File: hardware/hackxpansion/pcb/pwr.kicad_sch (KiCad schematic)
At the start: 18 parts, among them Q2 2N7002, SW3 SW_On_Off, U5 SPX3819M5-L-3-3, U7 BQ24075RGT

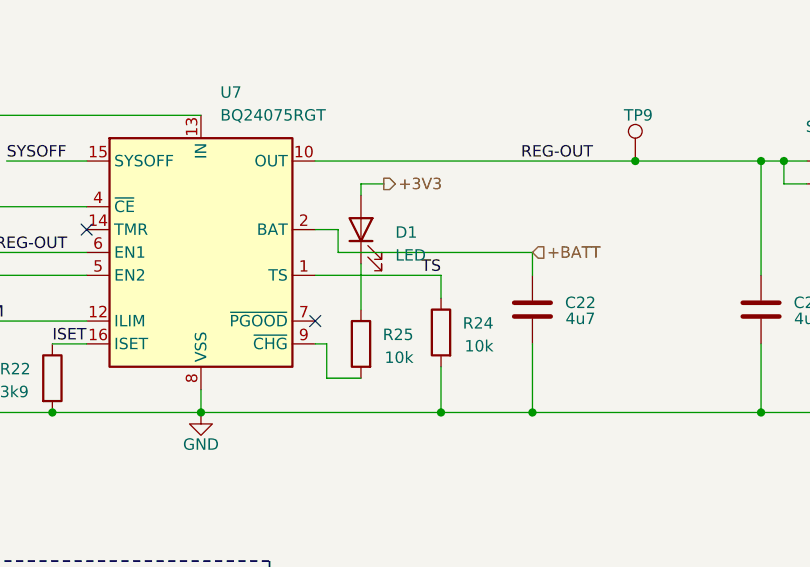
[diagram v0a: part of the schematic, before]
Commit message: updated led resistor
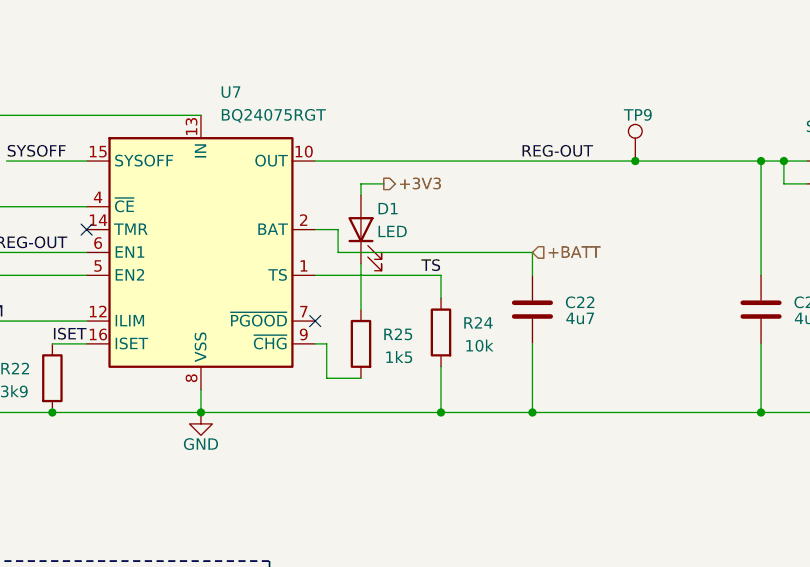
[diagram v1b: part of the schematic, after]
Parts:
- R25: value 10k -> 1k5; LCSC C25744 -> C25867
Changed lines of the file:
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@@
 			)
 		)
-		(property "Value" "10k"
+		(property "Value" "1k5"
 			(at 104.902 70.104 0)
 			(show_name no)
@@
 			)
 		)
-		(property "LCSC" "C25744"
+		(property "LCSC" "C25867"
 			(at 99.06 68.58 0)
 			(hide yes)
@@
 		(in_pos_files yes)
 		(dnp no)
-		(fields_autoplaced yes)
 		(property "Reference" "D1"
-			(at 102.87 56.1974 90)
+			(at 100.838 53.594 90)
 			(show_name no)
 			(do_not_autoplace no)
@@
 		)
 		(property "Value" "LED"
-			(at 102.87 58.7374 90)
-			(show_name no)
-			(do_not_autoplace no)
+			(at 100.838 56.134 90)
+			(show_name no)
+			(do_not_autoplace no)

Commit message: changed bom, added v cut
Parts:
- C21, C22, C23, C24: LCSC C307423 -> C23733
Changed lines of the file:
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@@
 			)
 		)
-		(property "LCSC" "C307423"
+		(property "LCSC" "C23733"
 			(at 167.64 64.77 0)
 			(hide yes)
@@
 			)
 		)
-		(property "LCSC" "C307423"
+		(property "LCSC" "C23733"
 			(at 45.72 63.5 0)
 			(hide yes)
@@
 			)
 		)
-		(property "LCSC" "C307423"
+		(property "LCSC" "C23733"
 			(at 143.51 64.77 0)
 			(hide yes)
@@
 			)
 		)
-		(property "LCSC" "C307423"
+		(property "LCSC" "C23733"
 			(at 118.11 64.77 0)
 			(hide yes)

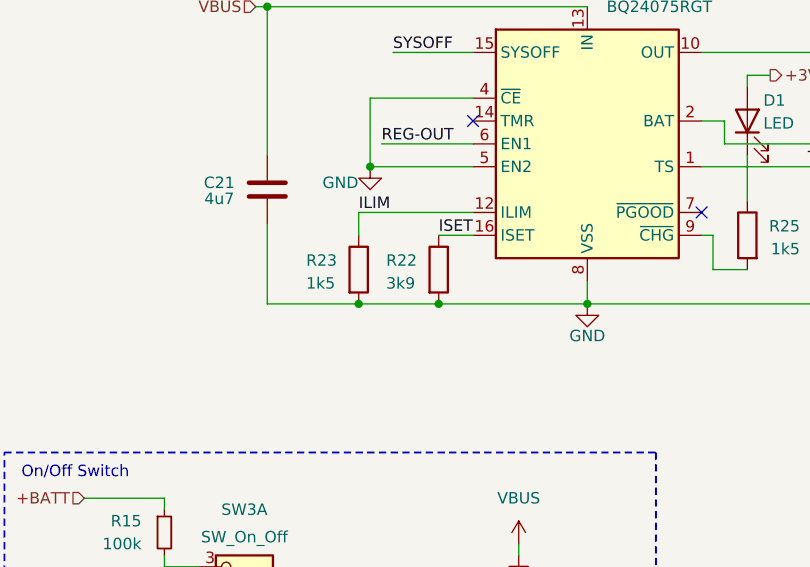
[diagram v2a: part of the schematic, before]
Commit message: updated part numbers
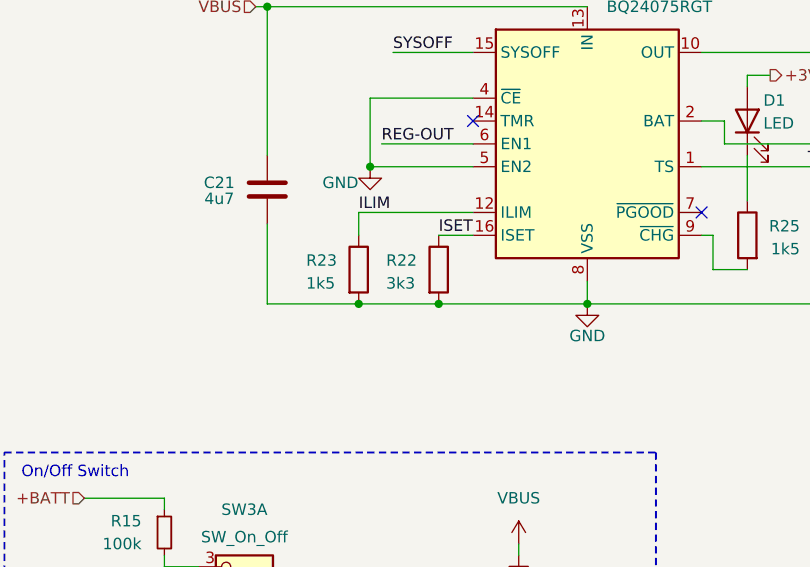
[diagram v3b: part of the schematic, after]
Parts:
- R22: value 3k9 -> 3k3; LCSC C131467 -> C25890
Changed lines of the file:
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@@
 			)
 		)
-		(property "Value" "3k9"
+		(property "Value" "3k3"
 			(at 58.928 73.914 0)
 			(show_name no)
@@
 			)
 		)
-		(property "LCSC" "C131467"
+		(property "LCSC" "C25890"
 			(at 64.77 72.39 0)
 			(hide yes)

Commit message: updated module detect resistor to 0.1%
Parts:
- R14: LCSC C2906861 -> C190095
- R24: LCSC C25744 -> C190095
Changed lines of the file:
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@@
 			)
 		)
-		(property "LCSC" "C2906861"
+		(property "LCSC" "C190095"
 			(at 73.66 118.11 0)
 			(hide yes)
@@
 			)
 		)
-		(property "LCSC" "C25744"
+		(property "LCSC" "C190095"
 			(at 107.95 67.31 0)
 			(hide yes)
